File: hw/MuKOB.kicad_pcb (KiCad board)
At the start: 4 copper layers, 123.2 x 125.7 mm, 135 parts, among them J1 UART0 IO01, J10 IO_EX, J11 SPKR_L, J12 SPKR_R, J13 UI 20-RBN, J14 AUDIO, J15 SPI-0, J16 SPI-DISP, J17 SW_MATRIX, J18 UIM 20-FCC, J19 UIM 20-RBN, J2 SERIAL-COMM, J3 KEY_SND_IF, J4 GPIO28, J5 I2C-0, J6 MicroSD-Socket w/Det, J7 KEY-PADDLE, J8 UART1 IO89, J9 UI 20-FCC, Q1 2N3904, SW1 RESET, SW2 RE-SO, SW3 UP, SW4 LF, SW5 EN, SW6 RT, SW7 DN, SW8 RE-AO, SW9 RE-BO, U1 MAX3221, U2 PicoW, U3 MCP23S08-E/SO, U4 TLV70033_SOT23-5, U5 TPA2012D2RTJT, U6 NC7WZ16P6X

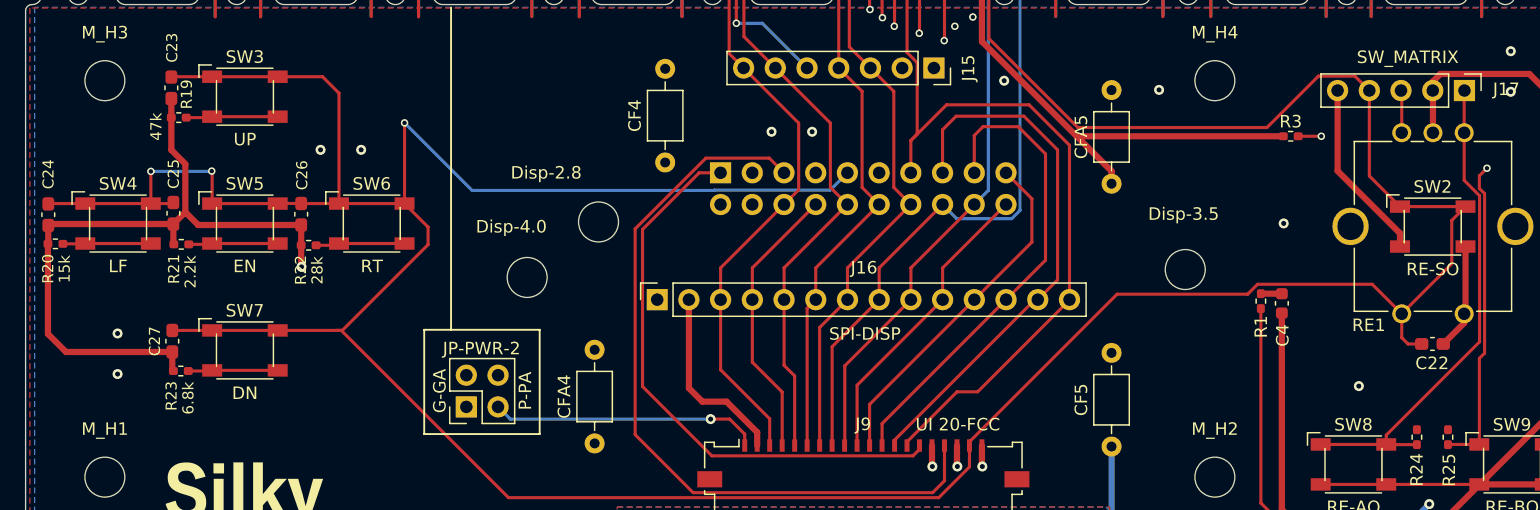
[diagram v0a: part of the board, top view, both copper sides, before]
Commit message: KS-MkIV: Pinout for bridge and mini-sounder update.
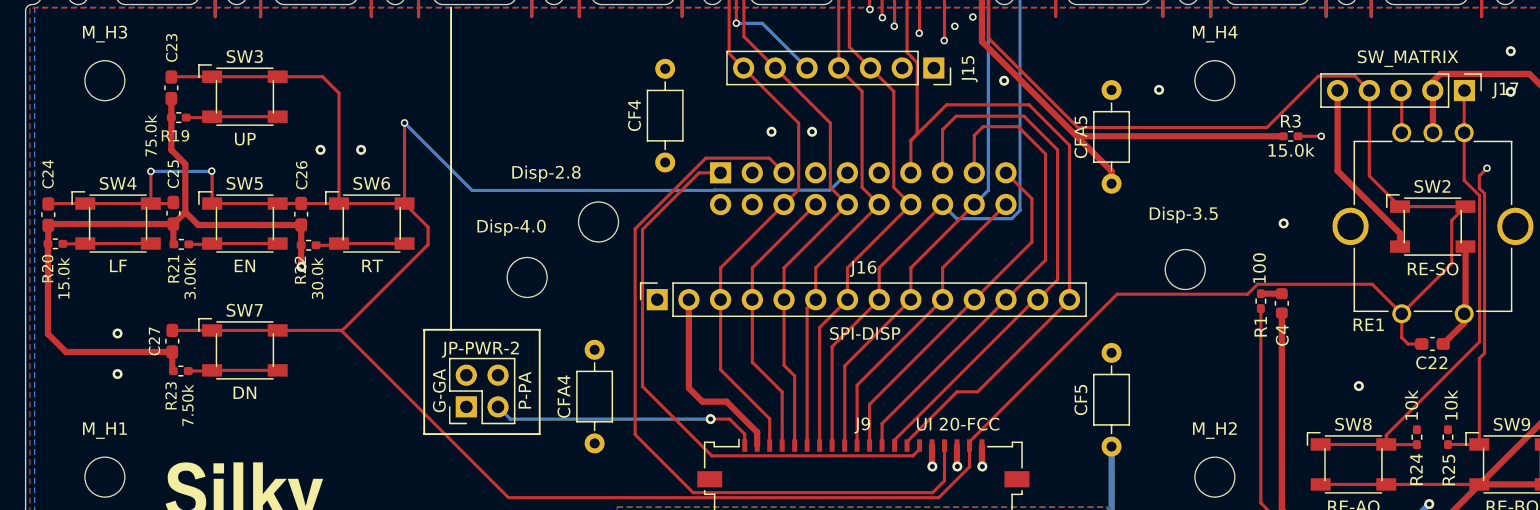
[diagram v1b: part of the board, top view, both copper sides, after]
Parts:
- R19: value 47k -> 75.0k
- R20: value 15k -> 15.0k
- R21: value 2.2k -> 3.00k
- R22: value 28k -> 30.0k
- R23: value 6.8k -> 7.50k
- R3: value 10k -> 15.0k
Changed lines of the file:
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@@
   (title_block
     (title "MuKOB Main Board")
-    (rev "1.0")
+    (rev "1.0a")
     (company "Silky Design")
-    (comment 1 "Copyright AESilky 2023")
+    (comment 1 "Copyright AESilky 2023-24")
+    (comment 4 "a=Value/Silkscreen Changes only")
   )
   (layers
@@
     (property "ki_keywords" "R res resistor")
     (attr smd)
-    (fp_text reference "R19" (at 0.6349 -1.8646 90) (layer "F.SilkS")
+    (fp_text reference "R19" (at -0.2794 1.4882) (layer "F.SilkS")
         (effects (font (size 0.889 0.889) (thickness 0.15)))
     )
-    (fp_text value "47k" (at -1.8035 0.7262 90) (layer "F.SilkS")
+    (fp_text value "75.0k" (at -2.1844 1.4882 90) (layer "F.SilkS")
         (effects (font (size 0.889 0.889) (thickness 0.15)))
     )
@@
         (effects (font (size 0.889 0.889) (thickness 0.15)))
     )
-    (fp_text value "2.2k" (at 0.7366 2.2098 90) (layer "F.SilkS")
+    (fp_text value "3.00k" (at 0.7366 2.7686 90) (layer "F.SilkS")
         (effects (font (size 0.889 0.889) (thickness 0.15)))
     )
@@
         (effects (font (size 0.889 0.889) (thickness 0.15)))
     )
-    (fp_text value "6.8k" (at 0.5962 2.174 90) (layer "F.SilkS")
+    (fp_text value "7.50k" (at 0.5962 2.7836 90) (layer "F.SilkS")
         (effects (font (size 0.889 0.889) (thickness 0.15)))
     )
@@
         (effects (font (size 1 1) (thickness 0.15)))
     )
-    (fp_text value "10k" (at 0 1.17 90) (layer "F.Fab")
+    (fp_text value "10k" (at -2.5146 -0.3048 90) (layer "F.SilkS")
         (effects (font (size 1 1) (thickness 0.15)))
     )
@@
     (property "Sheetfile" "MuKOB.kicad_sch")
     (property "Sheetname" "")
+    (property "exclude_from_bom" "")
     (property "ki_description" "Mounting Hole with connection")
     (property "ki_keywords" "mounting hole")
-    (attr exclude_from_pos_files)
+    (attr exclude_from_pos_files exclude_from_bom)
     (fp_text reference "M_KSI3" (at 0 -3.85) (layer "F.SilkS")
         (effects (font (size 1 1) (thickness 0.15)))
@@
         (effects (font (size 1 1) (thickness 0.15)))
     )
-    (fp_text value "10k" (at 0 1.17 90) (layer "F.Fab")
+    (fp_text value "10k" (at -2.5146 0.381 90) (layer "F.SilkS")
         (effects (font (size 1 1) (thickness 0.15)))
     )
@@
     (property "Sheetfile" "MuKOB.kicad_sch")
     (property "Sheetname" "")
+    (property "exclude_from_bom" "")
     (property "ki_description" "Mounting Hole with connection")
     (property "ki_keywords" "mounting hole")
-    (attr exclude_from_pos_files)
+    (attr exclude_from_pos_files exclude_from_bom)
     (fp_text reference "M_KSI4" (at 0 -3.85) (layer "F.SilkS")
         (effects (font (size 1 1) (thickness 0.15)))
@@
         (effects (font (size 1 1) (thickness 0.15)))
     )
-    (fp_text value "10k" (at 0 1.17) (layer "F.Fab")
+    (fp_text value "15.0k" (at 0 1.17) (layer "F.SilkS")
         (effects (font (size 1 1) (thickness 0.15)))
     )
@@
         (effects (font (size 0.889 0.889) (thickness 0.15)))
     )
-    (fp_text value "15k" (at 0.7365 2.0216 90) (layer "F.SilkS")
+    (fp_text value "15.0k" (at 0.7111 2.809 90) (layer "F.SilkS")
         (effects (font (size 0.889 0.889) (thickness 0.15)))
     )
@@
         (effects (font (size 0.889 0.889) (thickness 0.15)))
     )
-    (fp_text value "28k" (at 0.6991 2.0066 90) (layer "F.SilkS")
+    (fp_text value "30.0k" (at 0.7499 2.6924 90) (layer "F.SilkS")
         (effects (font (size 0.889 0.889) (thickness 0.15)))
     )
@@
     (property "Sheetfile" "MuKOB.kicad_sch")
     (property "Sheetname" "")
+    (property "exclude_from_bom" "")
     (property "ki_description" "Mounting Hole with connection")
     (property "ki_keywords" "mounting hole")
-    (attr exclude_from_pos_files)
+    (attr exclude_from_pos_files exclude_from_bom)
     (fp_text reference "M_KSI2" (at 0 -3.85) (layer "F.SilkS")
         (effects (font (size 1 1) (thickness 0.15)))
@@
         (effects (font (size 1 1) (thickness 0.15)))
     )
-    (fp_text value "100" (at -2.6162 0.0762 90) (layer "F.Fab")
+    (fp_text value "100" (at -2.6162 0.0762 90) (layer "F.SilkS")
         (effects (font (size 1 1) (thickness 0.15)))
     )
@@
     (property "Sheetfile" "MuKOB.kicad_sch")
     (property "Sheetname" "")
+    (property "exclude_from_bom" "")
     (property "ki_description" "Mounting Hole with connection")
     (property "ki_keywords" "mounting hole")
-    (attr exclude_from_pos_files)
+    (attr exclude_from_pos_files exclude_from_bom)
     (fp_text reference "M_KSI1" (at 0 -3.85) (layer "F.SilkS")
         (effects (font (size 1 1) (thickness 0.15)))
